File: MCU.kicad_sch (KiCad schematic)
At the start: 27 parts, among them J1 USB_B_Micro, J2 Conn_01x02, U1 NCP1117-3.3_SOT223, U2 W25Q128JVS, U3 RP2040, Y1 ABLS-12.000MHZ-B4-T

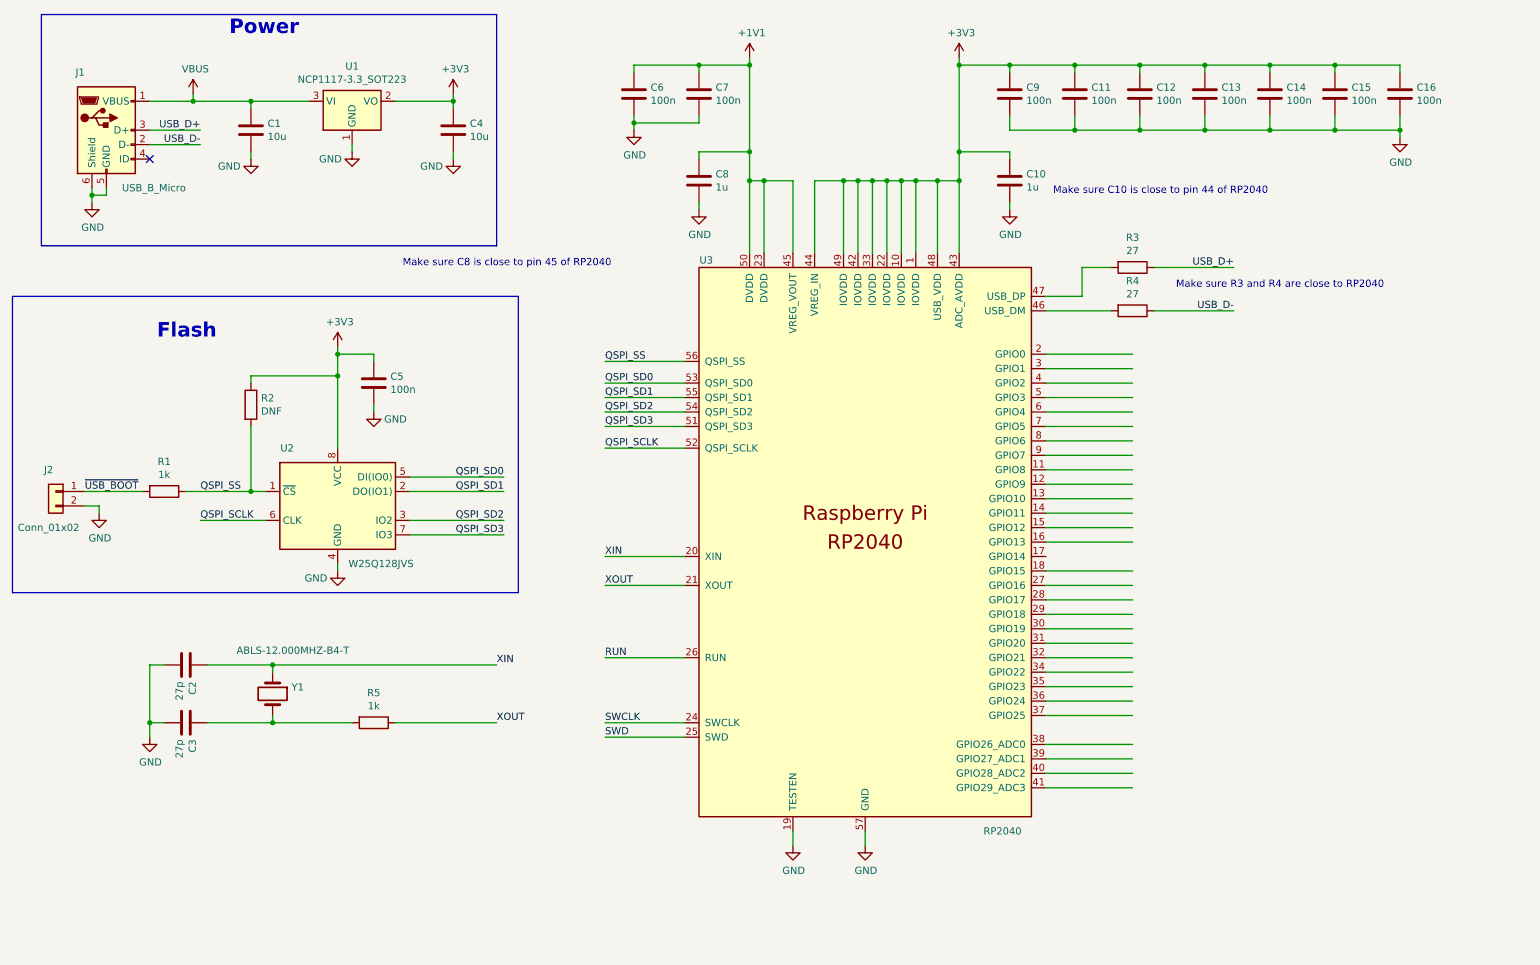
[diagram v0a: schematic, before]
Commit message: Remove dup folder
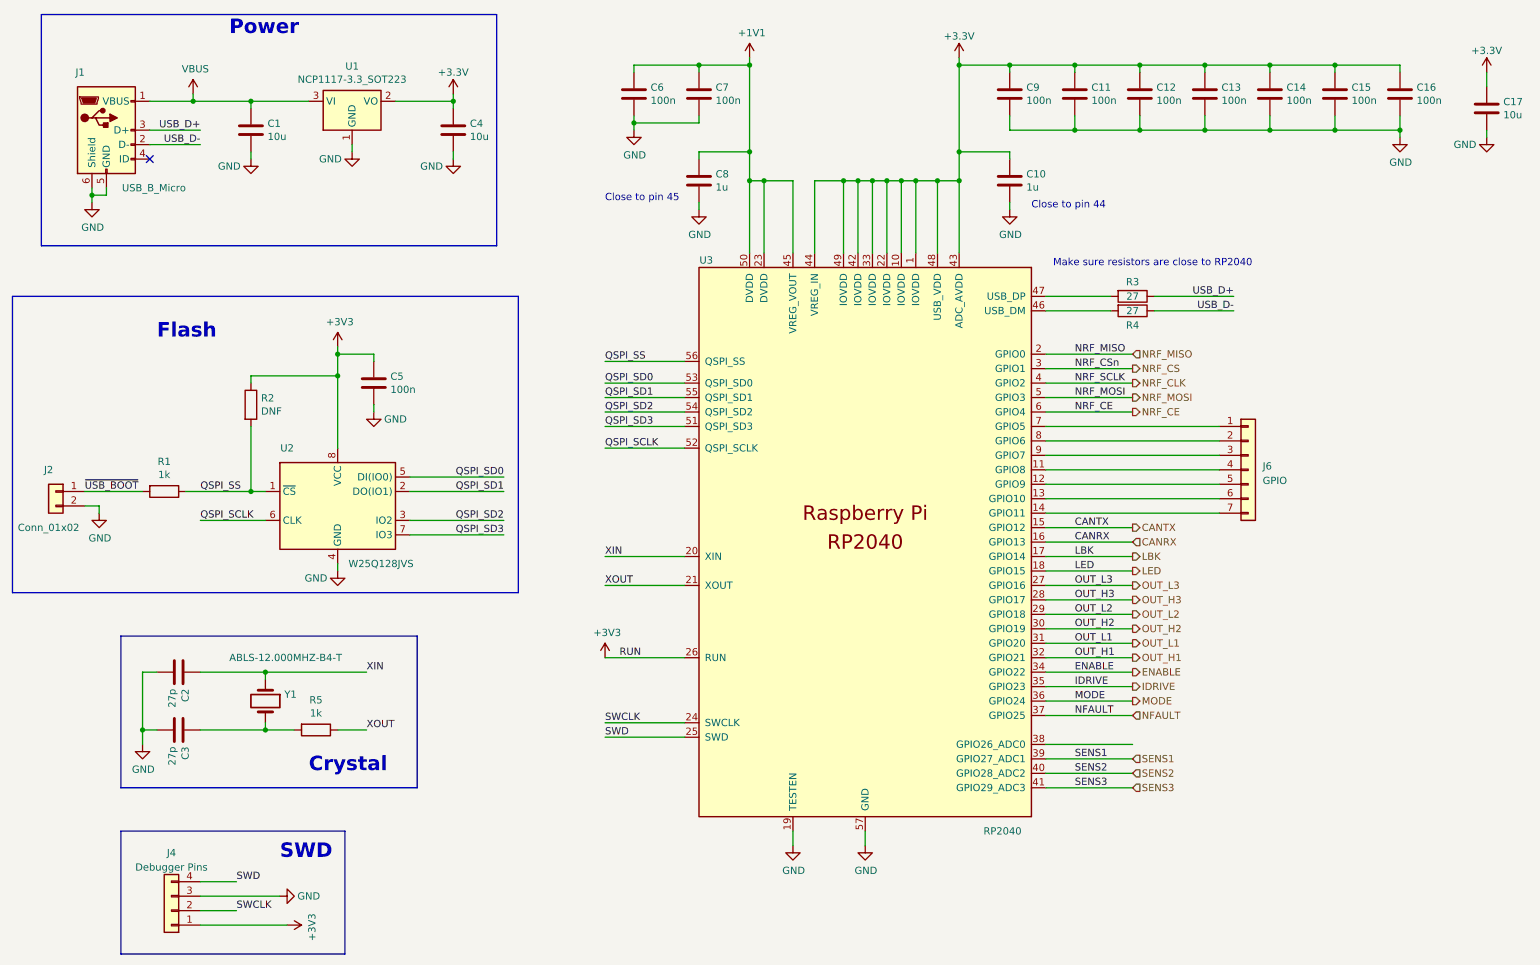
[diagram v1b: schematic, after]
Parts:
- added C17: 10u, Capacitor_SMD:C_0805_2012Metric, symbol Device:C
- added J4: Debugger Pins, symbol Connector_Generic:Conn_01x04
- added J6: GPIO, Connector_PinSocket_2.54mm:PinSocket_1x07_P2.54mm_Vertical, symbol Connector_Generic:Conn_01x07
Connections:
- net RUN is gone; now on net +3V3: U3.26 (RUN)
- net +3V3: now also J4.1 (Pin_1); no longer C10.1, C11.1, C12.1, C13.1, C14.1, C15.1, C16.1, C4.1, C9.1, U1.2 (VO), U3.1 (IOVDD), U3.10 (IOVDD), U3.22 (IOVDD), U3.33 (IOVDD), U3.42 (IOVDD), U3.43 (ADC_AVDD), U3.44 (VREG_IN), U3.48 (USB_VDD), U3.49 (IOVDD)
- net GND: now also C17.2, J4.3 (Pin_3)
- net SWCLK: now also J4.2 (Pin_2)
- net SWD: now also J4.4 (Pin_4)
- net at U3.11 (GPIO8): now also J6.4 (Pin_4)
- net at U3.12 (GPIO9): now also J6.5 (Pin_5)
- net at U3.13 (GPIO10): now also J6.6 (Pin_6)
- net at U3.14 (GPIO11): now also J6.7 (Pin_7)
- net CANTX: now reaches U3.15 (GPIO12)
- net CANRX: now reaches U3.16 (GPIO13)
- net LBK: now reaches U3.17 (GPIO14)
- net LED: now reaches U3.18 (GPIO15)
- net NRF_MISO: now reaches U3.2 (GPIO0)
- net OUT_L3: now reaches U3.27 (GPIO16)
- net OUT_H3: now reaches U3.28 (GPIO17)
- net OUT_L2: now reaches U3.29 (GPIO18)
- net NRF_CS: now reaches U3.3 (GPIO1)
- net OUT_H2: now reaches U3.30 (GPIO19)
- net OUT_L1: now reaches U3.31 (GPIO20)
- net OUT_H1: now reaches U3.32 (GPIO21)
- net ENABLE: now reaches U3.34 (GPIO22)
- net IDRIVE: now reaches U3.35 (GPIO23)
- net MODE: now reaches U3.36 (GPIO24)
- net NFAULT: now reaches U3.37 (GPIO25)
- net SENS1: now reaches U3.39 (GPIO27_ADC1)
- net NRF_CLK: now reaches U3.4 (GPIO2)
- net SENS2: now reaches U3.40 (GPIO28_ADC2)
- net SENS3: now reaches U3.41 (GPIO29_ADC3)
- net NRF_MOSI: now reaches U3.5 (GPIO3)
- net NRF_CE: now reaches U3.6 (GPIO4)
- net at U3.7 (GPIO5): now also J6.1 (Pin_1)
- net at U3.8 (GPIO6): now also J6.2 (Pin_2)
- net at U3.9 (GPIO7): now also J6.3 (Pin_3)
- new net +3.3V: C10.1, C11.1, C12.1, C13.1, C14.1, C15.1, C16.1, C17.1, C4.1, C9.1, U1.2 (VO), U3.1 (IOVDD), U3.10 (IOVDD), U3.22 (IOVDD), U3.33 (IOVDD), U3.42 (IOVDD), U3.43 (ADC_AVDD), U3.44 (VREG_IN), U3.48 (USB_VDD), U3.49 (IOVDD)
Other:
- note added: "Close to pin 44"
- note added: "Close to pin 45"
- note added: "Crystal"
- note added: "Make sure resistors are close to RP2040"
- note added: "SWD"
- note removed: "Make sure C10 is close to pin 44 of RP2040"
- note removed: "Make sure C8 is close to pin 45 of RP2040"
- note removed: "Make sure R3 and R4 are close to RP2040"
- moved on the sheet: C2, C3, R3, R5, Y1

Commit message: Fix a few errors
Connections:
- net +3.3V: now also C5.1, R2.1, U2.8 (VCC)
- net +3V3: no longer C5.1, R2.1, U2.8 (VCC)
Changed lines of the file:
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@@
+    )
+  )
+  (symbol (lib_id "power:+3.3V") (at 72.39 77.47 0) (unit 1)
+    (in_bom yes) (on_board yes) (dnp no) (fields_autoplaced)
+    (property "Reference" "#PWR022" (at 72.39 81.28 0)
+      (effects (font (size 1.27 1.27)) hide)
+    )
+    (property "Value" "+3.3V" (at 72.39 73.66 0)
+      (effects (font (size 1.27 1.27)))
+    )
+    (property "Footprint" "" (at 72.39 77.47 0)
+      (effects (font (size 1.27 1.27)) hide)
+    )
+    (property "Datasheet" "" (at 72.39 77.47 0)
+      (effects (font (size 1.27 1.27)) hide)
+    )
+    (pin "1")
+    (instances
+      (project "electrium-esc-v2"
+        (path "/be00c12c-11fa-42cb-8a0b-46fcd24b2ced/3a1c0a34-127f-4b4c-9fd7-3b3e53fd2f6f"
+          (reference "#PWR022") (unit 1)
+        )
+      )
     )
   )
@@
         )
       )
-    )
-  )
-  (symbol (lib_id "power:+3V3") (at 72.39 77.47 0) (unit 1)
-    (in_bom yes) (on_board yes) (dnp no)
-    (property "Reference" "#PWR07" (at 72.39 81.28 0)
-      (effects (font (size 1.27 1.27)) hide)
-    )
-    (property "Value" "+3V3" (at 72.771 73.0758 0)
-      (effects (font (size 1.27 1.27)))
-    )
-    (property "Footprint" "" (at 72.39 77.47 0)
-      (effects (font (size 1.27 1.27)) hide)
-    )
-    (property "Datasheet" "" (at 72.39 77.47 0)
-      (effects (font (size 1.27 1.27)) hide)
-    )
-    (pin "1")
-    (instances
-      (project "RP2040_minimal"
-        (path "/6531fadb-24de-4a4f-a44d-3d13e31f0217"
-          (reference "#PWR07") (unit 1)
-        )
-      )
-      (project "electrium-esc-v2"
-        (path "/be00c12c-11fa-42cb-8a0b-46fcd24b2ced/3a1c0a34-127f-4b4c-9fd7-3b3e53fd2f6f"
-          (reference "#PWR022") (unit 1)
-        )
-      )

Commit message: Add reference changes
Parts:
- C?: renamed from C13; footprint Capacitor_SMD:C_0402_1005Metric -> Capacitor_SMD:C_0603_1608Metric
- C?: renamed from C2; footprint Capacitor_SMD:C_0402_1005Metric -> Capacitor_SMD:C_0603_1608Metric
- C?: renamed from C14; footprint Capacitor_SMD:C_0402_1005Metric -> Capacitor_SMD:C_0603_1608Metric
- C?: renamed from C17; footprint Capacitor_SMD:C_0805_2012Metric -> Capacitor_THT:CP_Radial_D5.0mm_P2.00mm
- C?: renamed from C3; footprint Capacitor_SMD:C_0402_1005Metric -> Capacitor_SMD:C_0603_1608Metric
- C?: renamed from C7; footprint Capacitor_SMD:C_0402_1005Metric -> Capacitor_SMD:C_0603_1608Metric
- C?: renamed from C16; footprint Capacitor_SMD:C_0402_1005Metric -> Capacitor_SMD:C_0603_1608Metric
- C?: renamed from C12; footprint Capacitor_SMD:C_0402_1005Metric -> Capacitor_SMD:C_0603_1608Metric
- C?: renamed from C15; footprint Capacitor_SMD:C_0402_1005Metric -> Capacitor_SMD:C_0603_1608Metric
- C?: renamed from C4; footprint Capacitor_SMD:C_0805_2012Metric -> Capacitor_SMD:C_0603_1608Metric
- C?: renamed from C5; footprint Capacitor_SMD:C_0402_1005Metric -> Capacitor_SMD:C_0603_1608Metric
- C?: renamed from C1; footprint Capacitor_SMD:C_0805_2012Metric -> Capacitor_SMD:C_0603_1608Metric
- C?: renamed from C9; footprint Capacitor_SMD:C_0402_1005Metric -> Capacitor_SMD:C_0603_1608Metric
- C?: renamed from C6; footprint Capacitor_SMD:C_0402_1005Metric -> Capacitor_SMD:C_0603_1608Metric
- C?: renamed from C11; footprint Capacitor_SMD:C_0402_1005Metric -> Capacitor_SMD:C_0603_1608Metric
- C?: renamed from C8; footprint Capacitor_SMD:C_0402_1005Metric -> Capacitor_SMD:C_0603_1608Metric
- C?: renamed from C10; footprint Capacitor_SMD:C_0402_1005Metric -> Capacitor_SMD:C_0603_1608Metric
- J4: footprint (none) -> Connector_JST:JST_XH_B4B-XH-A_1x04_P2.50mm_Vertical
- J?: renamed from J1; footprint RP2040_minimal:USB_Micro-B_Amphenol_10103594-0001LF_Horizontal_modified -> Connector_USB:USB_Micro-B_Molex-105017-0001
- R?: renamed from R2; footprint Capacitor_SMD:C_0402_1005Metric -> Resistor_SMD:R_0603_1608Metric
- R?: renamed from R3; footprint Capacitor_SMD:C_0402_1005Metric -> Resistor_SMD:R_0603_1608Metric
- R?: renamed from R1; footprint Capacitor_SMD:C_0402_1005Metric -> Resistor_SMD:R_0603_1608Metric
- R?: renamed from R4; footprint Capacitor_SMD:C_0402_1005Metric -> Resistor_SMD:R_0603_1608Metric
- R?: renamed from R5; footprint Capacitor_SMD:C_0402_1005Metric -> Resistor_SMD:R_0603_1608Metric
- U?: renamed from U3; footprint RP2040_minimal:RP2040-QFN-56 -> ext_footprint:RP2040-QFN-56
- Y?: renamed from Y1; footprint RP2040_minimal:Crystal_SMD_HC49-US -> ext_footprint:Crystal_SMD_HC49-US
- renumbered J6 to J5, J2 to J?, U1 to U?, U2 to U?
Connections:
- net +3V3 is gone; now on net +3.3V: J4.1 (Pin_1), U?.26 (RUN)
- no-connect marks 1 -> 2

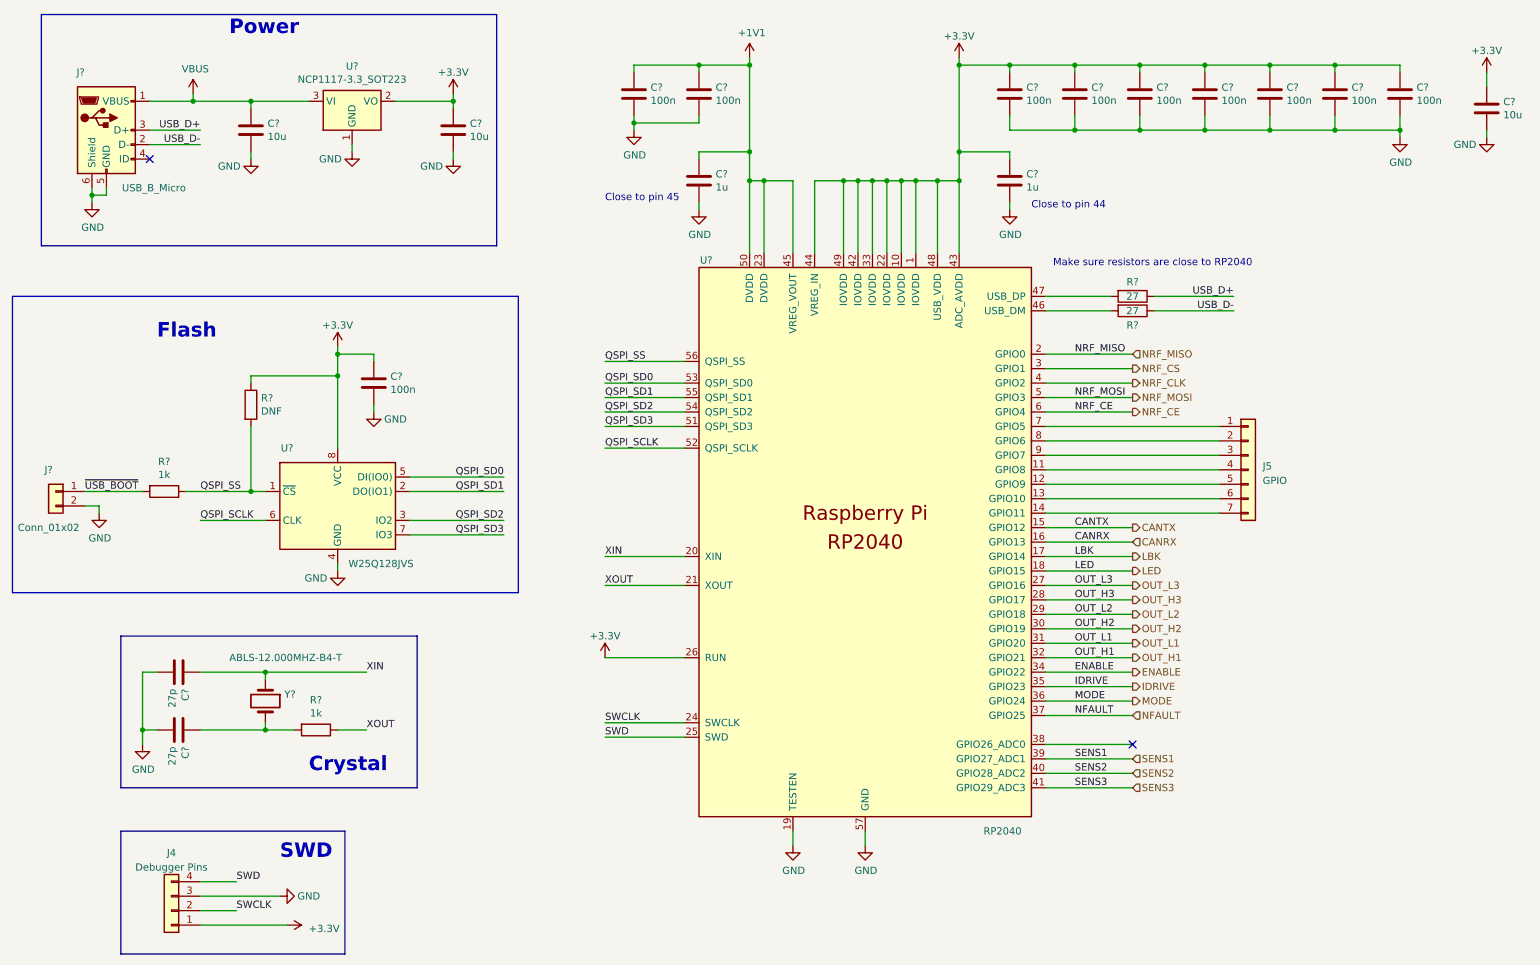
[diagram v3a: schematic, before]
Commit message: changed pins
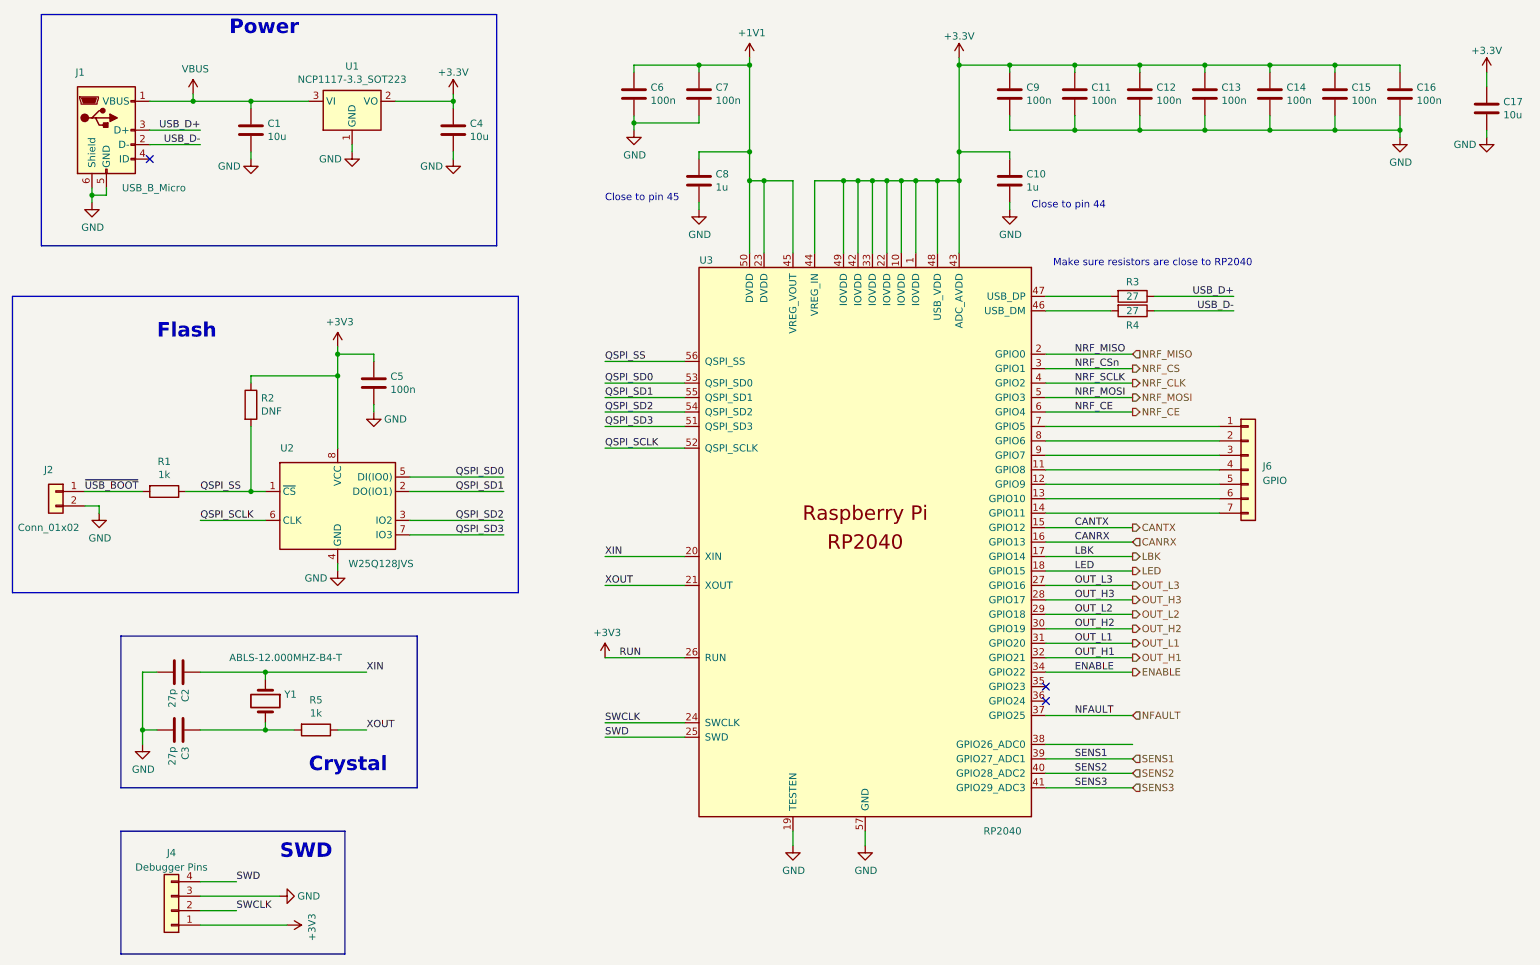
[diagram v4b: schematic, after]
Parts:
- C1, C4: renamed from C?; footprint Capacitor_SMD:C_0603_1608Metric -> Capacitor_SMD:C_0805_2012Metric
- C10, C11, C12, C13, C14, C15, C16, C2, C3, C5, C6, C7, C8, C9: renamed from C?; footprint Capacitor_SMD:C_0603_1608Metric -> Capacitor_SMD:C_0402_1005Metric
- C17: renamed from C?; footprint Capacitor_THT:CP_Radial_D5.0mm_P2.00mm -> Capacitor_SMD:C_0805_2012Metric
- J1: renamed from J?; footprint Connector_USB:USB_Micro-B_Molex-105017-0001 -> RP2040_minimal:USB_Micro-B_Amphenol_10103594-0001LF_Horizontal_modified
- J4: footprint Connector_JST:JST_XH_B4B-XH-A_1x04_P2.50mm_Vertical -> (none)
- R1, R2, R3, R4, R5: renamed from R?; footprint Resistor_SMD:R_0603_1608Metric -> Capacitor_SMD:C_0402_1005Metric
- U3: renamed from U?; footprint ext_footprint:RP2040-QFN-56 -> RP2040_minimal:RP2040-QFN-56
- Y1: renamed from Y?; footprint ext_footprint:Crystal_SMD_HC49-US -> RP2040_minimal:Crystal_SMD_HC49-US
- gave numbers to parts that had none: 3
- renumbered J5 to J6
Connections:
- net +3.3V: no longer C5.1, J4.1 (Pin_1), R2.1, U2.8 (VCC), U3.26 (RUN)
- net IDRIVE: no longer names the net of U3.35 (GPIO23)
- net MODE: no longer names the net of U3.36 (GPIO24)
- new net +3V3: C5.1, J4.1 (Pin_1), R2.1, U2.8 (VCC), U3.26 (RUN)
- no-connect marks 2 -> 3
